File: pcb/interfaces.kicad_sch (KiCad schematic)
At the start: 20 parts, among them J10 BM08B-SRSS-TB, J14 BM03B-SRSS-TB, J3 BM03B-SRSS-TB, J8 BM04B-SRSS-TB, J9 BM04B-SRSS-TB

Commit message: Minor silkscreen changes.
Updated 2222 footprint
Ready for next release
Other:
- title: Aquarius Hub -> Aquarius Node
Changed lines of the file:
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@@
 	(paper "A4")
 	(title_block
-		(title "Aquarius Hub")
+		(title "Aquarius Node")
 		(date "<<release-date>>")
 		(rev "<<tag>>")

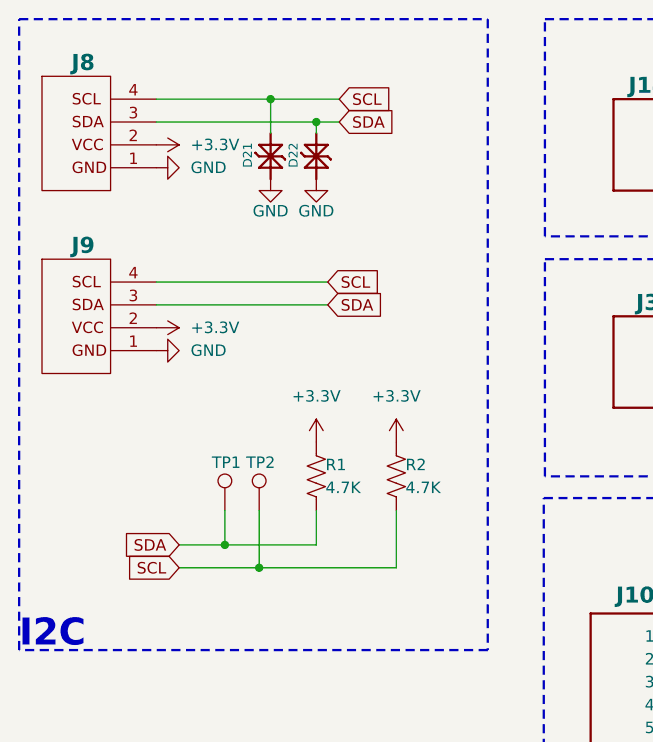
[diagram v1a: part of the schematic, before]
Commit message: Temoved duplicative test points
Cleaned up routing and silkscreen.
Updated mounting holes and tied to ground.
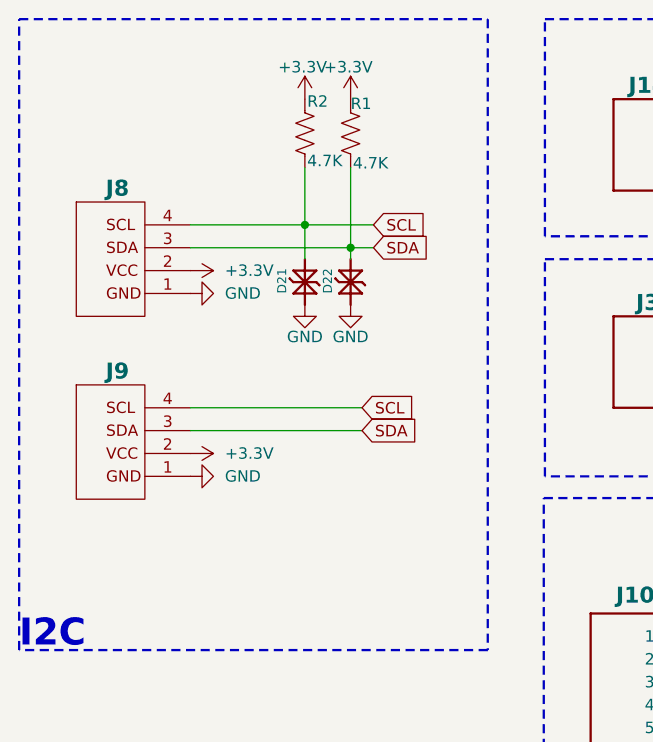
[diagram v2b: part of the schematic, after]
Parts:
- removed TP1, TP2: ~, CRGM Mechanical:TestPoint_Pad_D1.0mm, symbol Connector:TestPoint
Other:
- moved on the sheet: D21, D22, J8, J9, R1, R2

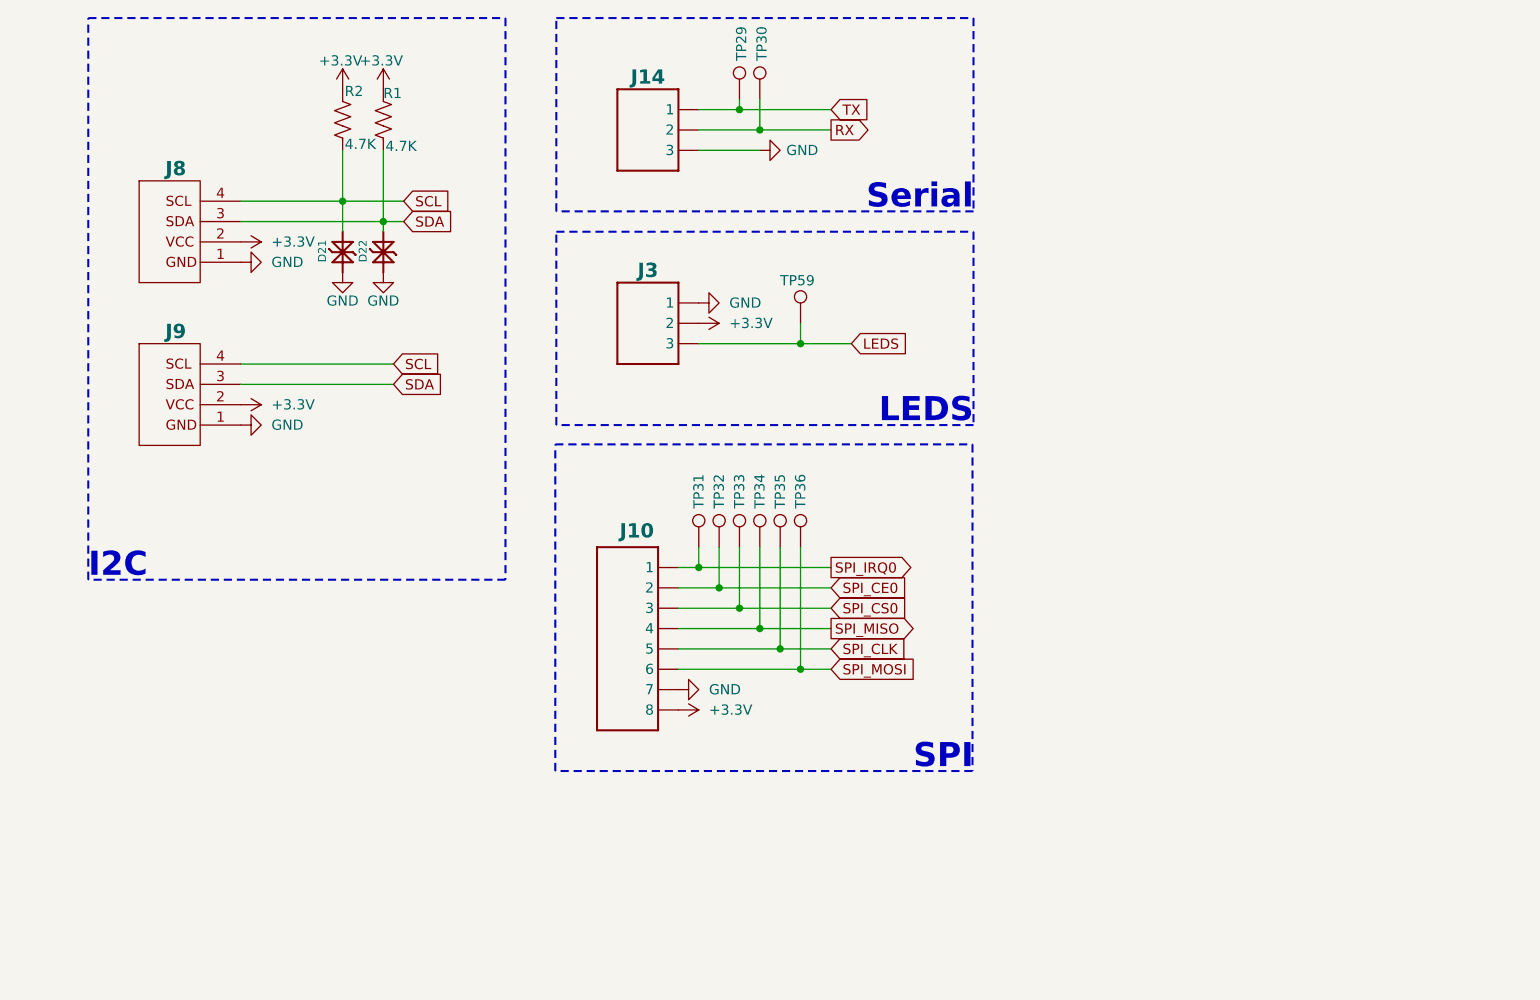
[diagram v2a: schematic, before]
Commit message: Added TVS to LED and Serial
Minor silkscreen updates
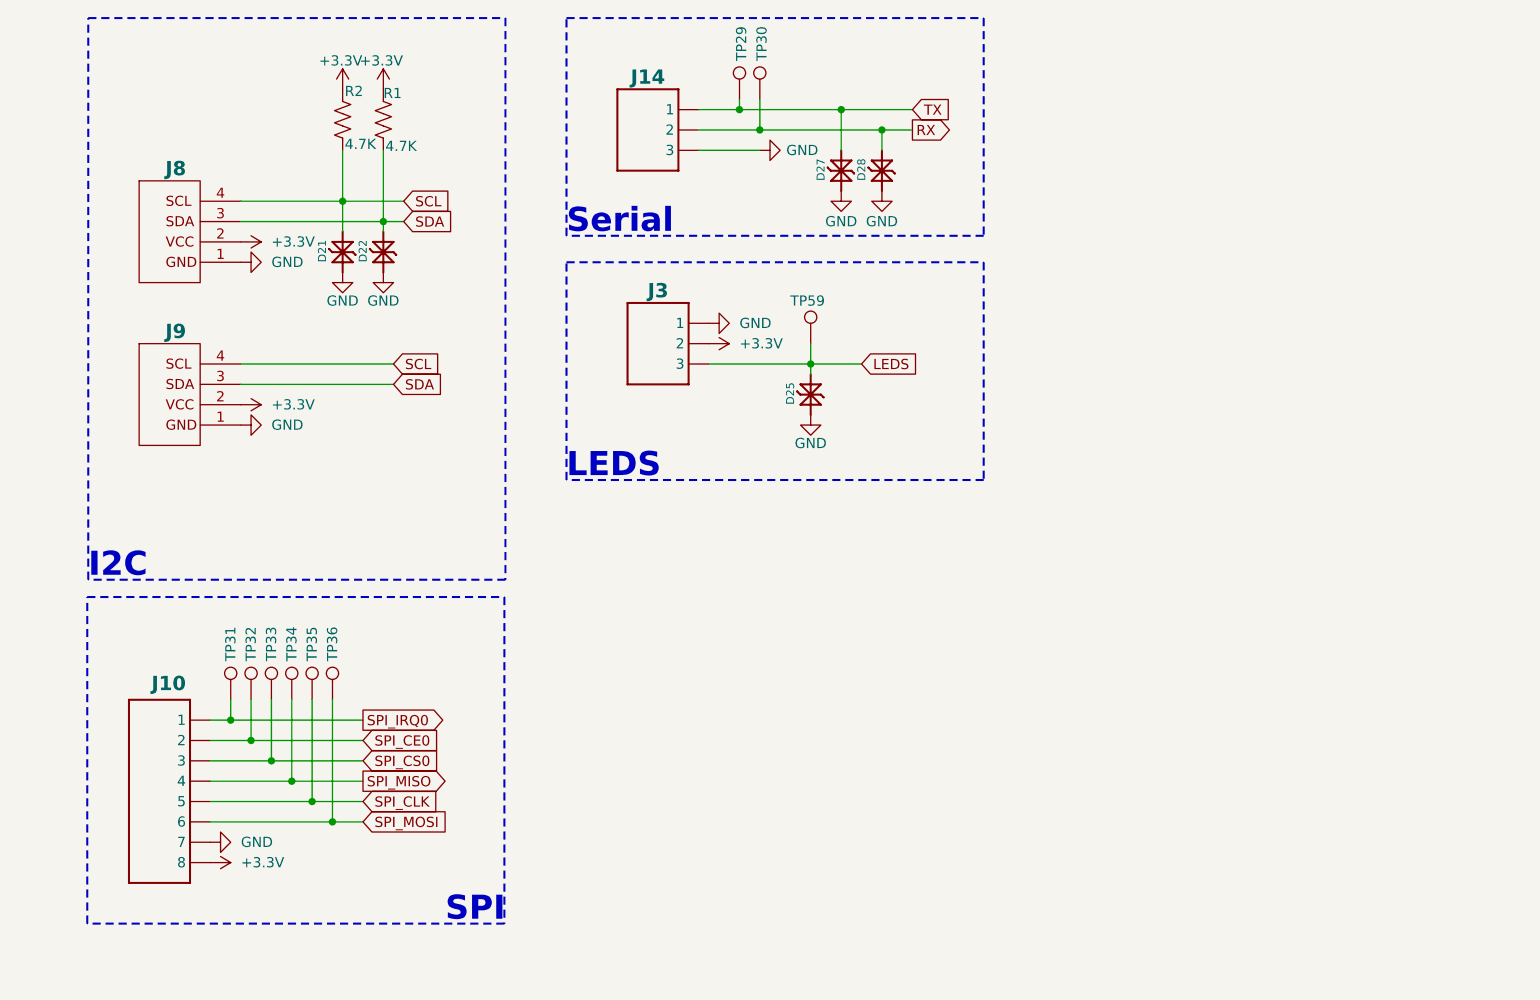
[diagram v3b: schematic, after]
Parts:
- added D25, D27, D28: PESD3V3S1BL, CRGM Passive:DFN1006-2, symbol CRGM Passive:PESD3V3S1BL
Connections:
- net GND: now also D25.1 (K1), D27.1 (K1), D28.1 (K1)
- net LEDS: now also D25.2 (K2)
- net RX: now also D28.2 (K2)
- net TX: now also D27.2 (K2)
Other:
- moved on the sheet: J10, J3, TP31, TP32, TP33, TP34, TP35, TP36, TP59

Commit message: Fixed part placement and missing model
Both display and 3.3 regulator were in the wrong place after updating from library!
LED was missing model
Minor silkscreen changes
Updated renders
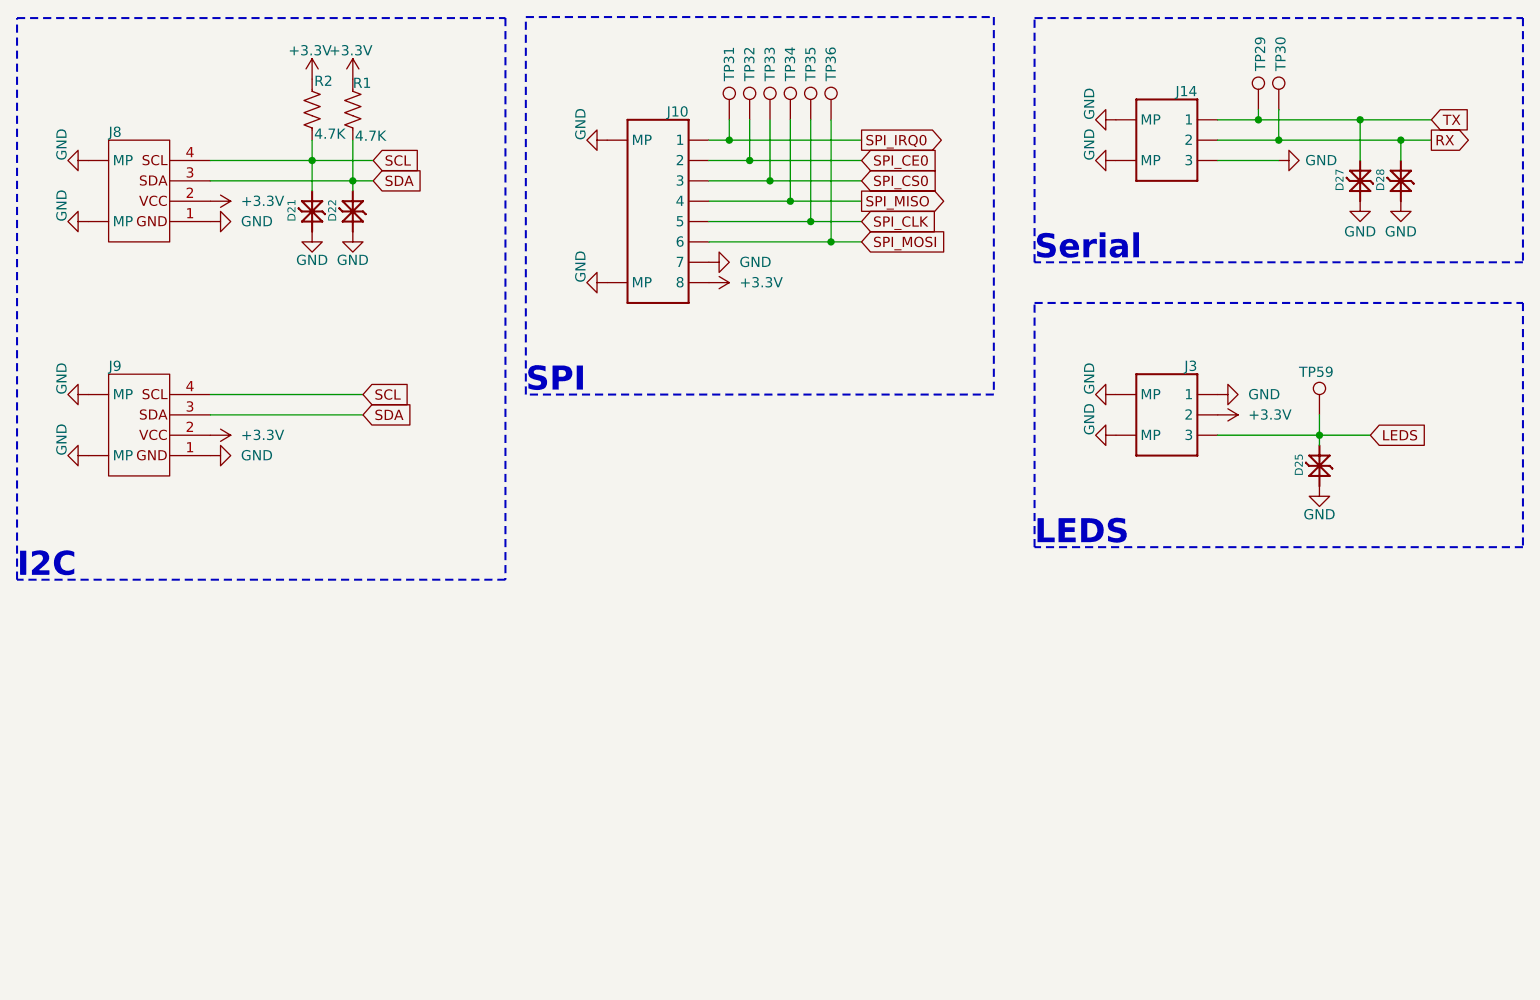
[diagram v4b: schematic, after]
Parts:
- J10: value BM08B-SRSS-TB -> ~
- J14, J3: value BM03B-SRSS-TB -> ~; LCSC C2904985 -> C2919601
- J8, J9: value BM04B-SRSS-TB -> ~; LCSC C2904986 -> C2919601
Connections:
- net GND: now also J10.MP, J14.MP, J3.MP, J8.MP, J9.MP
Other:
- moved on the sheet: D21, D22, D25, D27, D28, R1, R2, TP29, TP30, TP31, TP32, TP33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

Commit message: Updated foot prints and symbols
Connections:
- net GND: now also J10.0 (MP), J10.9 (MP), J14.0 (MP), J14.4 (MP), J3.0 (MP), J3.4 (MP), J8.0 (MP), J8.5 (MP), J9.0 (MP), J9.5 (MP); no longer J10.MP, J14.MP, J3.MP, J8.MP, J9.MP
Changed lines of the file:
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@@
 		(pin "2"
 		)
-		(pin "MP"
-		)
-		(pin "MP"
+		(pin "0"
+		)
+		(pin "5"
 		)
 		(instances
@@
 		(pin "1"
 		)
-		(pin "MP"
-		)
-		(pin "MP"
+		(pin "0"
+		)
+		(pin "4"
 		)
 		(instances
@@
 		(pin "8"
 		)
-		(pin "MP"
-		)
-		(pin "MP"
+		(pin "0"
+		)
+		(pin "9"
 		)
 		(instances
@@
 	)
 	(symbol
-		(lib_name "QWIIC_1")
 		(lib_id "CRGM Connector:QWIIC")
 		(at 36.83 30.48 0)
@@
 		(pin "2"
 		)
-		(pin "MP"
-		)
-		(pin "MP"
+		(pin "5"
+		)
+		(pin "0"
 		)
 		(instances
@@
 	)
 	(symbol
-		(lib_name "JST-SH-3_1")
 		(lib_id "CRGM Connector:JST-SH-3")
 		(at 172.72 62.23 0)
@@
 		(pin "1"
 		)
-		(pin "MP"
-		)
-		(pin "MP"
-		)
-		(instances
+		(pin "0"
+		)
+		(pin "4"
+		)
+		(instances

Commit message: Updated footprints and rotations
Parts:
- J14: Digikey 455-BM04B-SRSS-TBTR-ND -> 455-BM03B-SRSS-TBTR-ND; LCSC C2919601 -> C2904985; Mouser 306-BM04BSRSSTBTLFSN -> 306-BM03BSRSSTBTLFSN
- J3: Digikey 455-BM04B-SRSS-TBTR-ND -> 455-BM03B-SRSS-TBTR-ND; LCSC C2919601 -> C2904985; MPN BM04B-SRSS-TB -> BM03B-SRSS-TB; Mouser 306-BM04BSRSSTBTLFSN -> 306-BM03BSRSSTBTLFSN
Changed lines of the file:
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@@
 			)
 		)
-		(property "LCSC" "C2919601"
+		(property "LCSC" "C2904985"
 			(at 172.72 64.516 0)
 			(effects
@@
 			)
 		)
-		(property "Digikey" "455-BM04B-SRSS-TBTR-ND"
+		(property "Digikey" "455-BM03B-SRSS-TBTR-ND"
 			(at 172.72 59.944 0)
 			(effects
@@
 			)
 		)
-		(property "Mouser" "306-BM04BSRSSTBTLFSN"
+		(property "Mouser" "306-BM03BSRSSTBTLFSN"
 			(at 172.72 62.484 0)
 			(effects
@@
 			)
 		)
-		(property "LCSC" "C2919601"
+		(property "LCSC" "C2904985"
 			(at 172.72 98.806 0)
 			(effects
@@
 			)
 		)
-		(property "MPN" "BM04B-SRSS-TB"
+		(property "MPN" "BM03B-SRSS-TB"
 			(at 172.212 82.296 0)
 			(effects
@@
 			)
 		)
-		(property "Digikey" "455-BM04B-SRSS-TBTR-ND"
+		(property "Digikey" "455-BM03B-SRSS-TBTR-ND"
 			(at 172.72 94.234 0)
 			(effects
@@
 			)
 		)
-		(property "Mouser" "306-BM04BSRSSTBTLFSN"
+		(property "Mouser" "306-BM03BSRSSTBTLFSN"
 			(at 172.72 96.774 0)
 			(effects

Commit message: Fixed part numbers
Fixed 3 pin JST LCSC Part Number
Fixed MPN for JST 3 pin
Changed Hub to Node on top silkscreen
Updated renders
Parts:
- J14: MPN BM04B-SRSS-TB -> BM03B-SRSS-TB
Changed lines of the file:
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@@
 			)
 		)
-		(property "MPN" "BM04B-SRSS-TB"
+		(property "MPN" "BM03B-SRSS-TB"
 			(at 172.212 48.006 0)
 			(effects

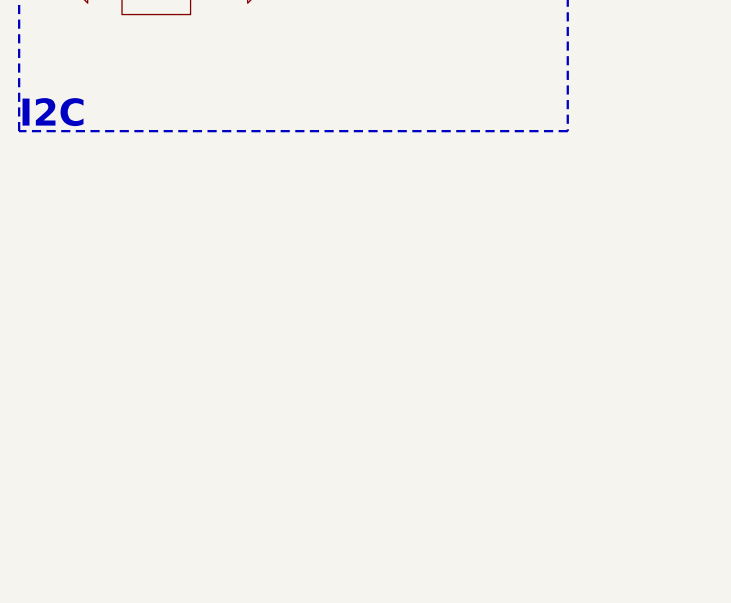
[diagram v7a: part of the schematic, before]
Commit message: Added analog port
re-routed
resized the pretty princess
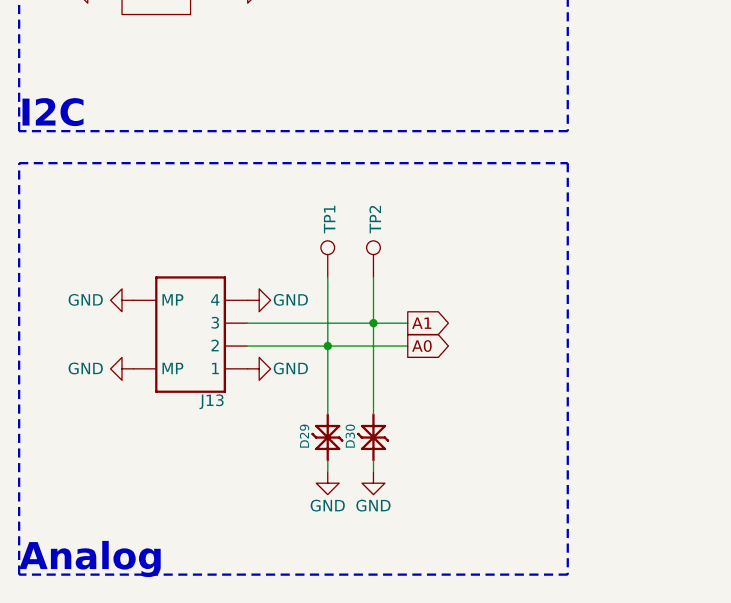
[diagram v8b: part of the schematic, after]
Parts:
- added D29, D30: PESD3V3S1BL, CRGM Passive:DFN1006-2, symbol CRGM Passive:PESD3V3S1BL
- added J13: ~, CRGM Connector:JST_SH_BM04B-SRSS-TB_1x04-1MP_P1.00mm_Vertical, symbol CRGM Connector:JST-SH-4
- added TP1, TP2: ~, CRGM Mechanical:TestPoint_Pad_D1.0mm, symbol Connector:TestPoint
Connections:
- net GND: now also D29.1 (K1), D30.1 (K1), J13.0 (MP), J13.1, J13.4, J13.5 (MP)
- new net A0: D29.2 (K2), J13.2, TP1.1
- new net A1: D30.2 (K2), J13.3, TP2.1
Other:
- note added: "Analog"
